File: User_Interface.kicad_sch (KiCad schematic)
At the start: 20 parts, among them SW1 SPST-NO, SW2 SPST-NO, U1 NC7WZ132L8X, U10 NC7WZ132L8X

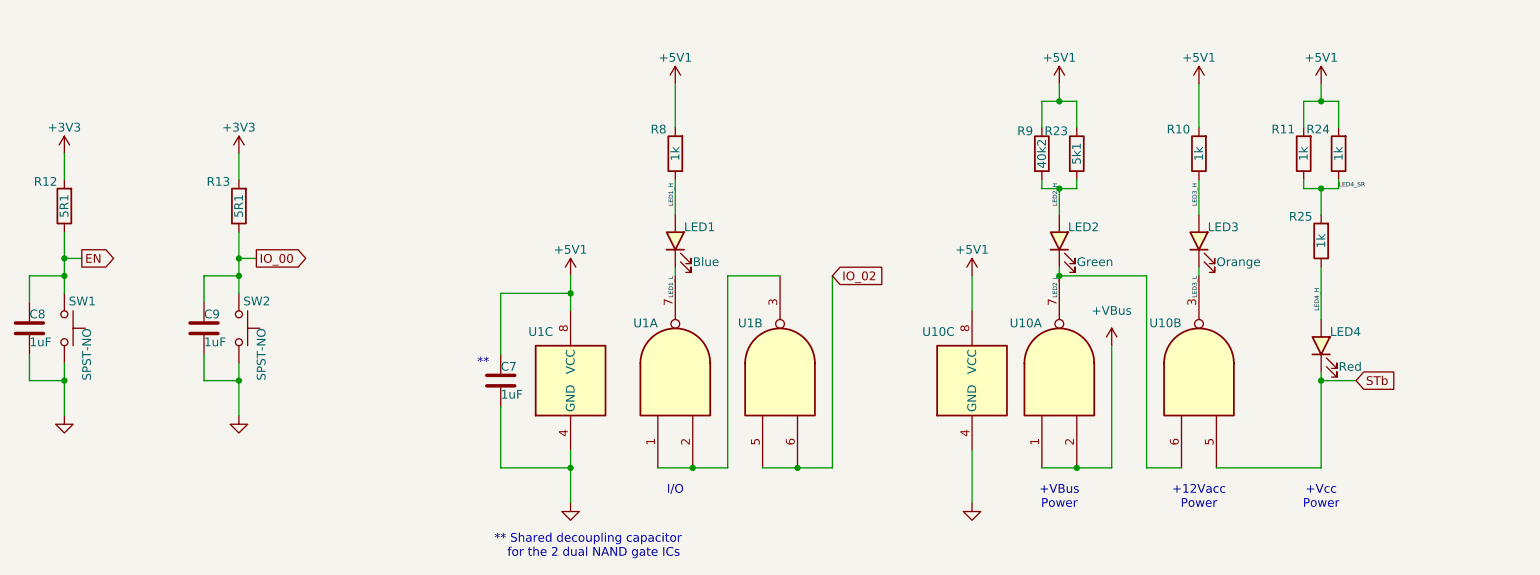
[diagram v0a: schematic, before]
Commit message: Update CAN_Interface.kicad_sch, ESP32-S3 Pico D1.kicad_dru, ESP32-S3 Pico D1.kicad_pcb, and 5 more files reroute completed
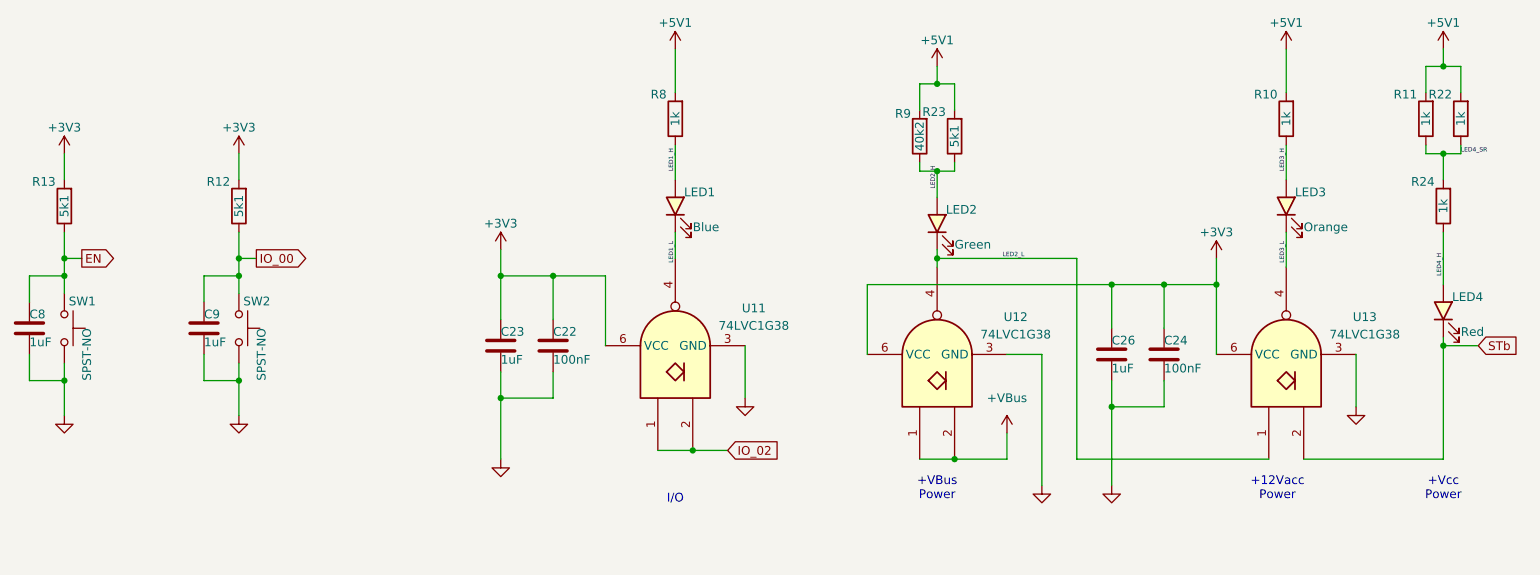
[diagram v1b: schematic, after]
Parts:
- removed C7: 1uF, Capacitors:C0201_Dense, symbol Device:C
- removed R25: 1k, Resistors:R0201_Dense, symbol Device:R
- removed U1, U10: NC7WZ132L8X, Personal_FootprintLibrary:UQFN8_1.6x1.6mm_P0.5, symbol PersonalSchematicSymbolLibrary:74xxx2G00
- added C22, C24: 100nF, Capacitors:C0201_Dense, symbol Device:C
- added C23, C26: 1uF, Capacitors:C0201_Dense, symbol Device:C
- added R22: 1k, Resistors:R0201_Dense, symbol Device:R
- added U11, U12, U13: 74LVC1G38, Personal_FootprintLibrary:DSF6, symbol 74xGxx:74LVC1G38
- R10, R11, R24, R8: Distributor Link 2 https://www.mouser.com/ProductDetail/Royalohm/PF01WMF5100TE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 -> https://www.mouser.com/ProductDetail/Royalohm/0201WMF1001TE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; LCSC C50670526 -> C270365; Manufacturer Part Number PF01WMF510KTEE -> 0201WMF1001TEE
- R12, R13: value 5R1 -> 5k1; Distributor Link 2 https://www.mouser.com/ProductDetail/Royalohm/PF01WMF5100TE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 -> https://www.mouser.com/ProductDetail/Royalohm/0201WMF5101TE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; LCSC C50670526 -> C270344; Manufacturer Part Number PF01WMF510KTEE -> 0201WMF5101TEE
- R23: Distributor Link 1 https://www.digikey.com/en/products/detail/yageo/AC0201FR-0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 -> (none); Distributor Link 2 https://www.mouser.com/ProductDetail/YAGEO/AC0201FR-0726K1L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 -> https://www.mouser.com/ProductDetail/Royalohm/0201WMF5101TE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; LCSC C910625 -> C270344; Manufacturer Yageo -> UNI-ROYAL(Uniroyal Elec); Manufacturer Part Number AC0201FR-0726K1L -> 0201WMF5101TEE
- R9: Distributor Link 1 https://www.digikey.com/en/products/detail/yageo/AC0201FR-0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 -> (none); Distributor Link 2 https://www.mouser.com/ProductDetail/YAGEO/AC0201FR-0726K1L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 -> https://www.mouser.com/ProductDetail/Royalohm/0201WMF4022TE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; LCSC C910625 -> C423536; Manufacturer Yageo -> UNI-ROYAL(Uniroyal Elec); Manufacturer Part Number AC0201FR-0726K1L -> 0201WMF4022TEE
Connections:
- net +3V3: now also C22.1, C23.1, C24.1, C26.1, U11.6 (VCC), U12.6 (VCC), U13.6 (VCC)
- net +5V1: now also R23.2, R9.2, R22.2; no longer R23.1, R24.2, R9.1
- net +VBus: now also U12.1, U12.2
- net EN: now also R13.1; no longer R12.1
- net GND: now also C22.2, C23.2, C24.2, C26.2, U11.3 (GND), U12.3 (GND), U13.3 (GND)
- net IO_00: now also R12.1; no longer R13.1
- net IO_02: now also U11.1, U11.2
- net LED1_L: now also U11.4
- net LED2_H: now also R23.1, R9.1; no longer R23.2, R9.2
- net LED2_L: now also U12.4, U13.1
- net LED3_L: now also U13.4
- net LED4_H: now also R24.1
- net LED4_SR: now also R24.2, R22.1; no longer R24.1
- net STb: now also U13.2
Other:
- note removed: "**"
- note removed: "** Shared decoupling capacitor for the 2 dual NAND gate ICs"
- moved on the sheet: LED1, LED2, LED3, LED4, R8
